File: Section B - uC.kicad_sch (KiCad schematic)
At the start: 9 parts, among them J1 Conn_ARM_SWD_TagConnect_TC203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, U1 ATtiny204-SS

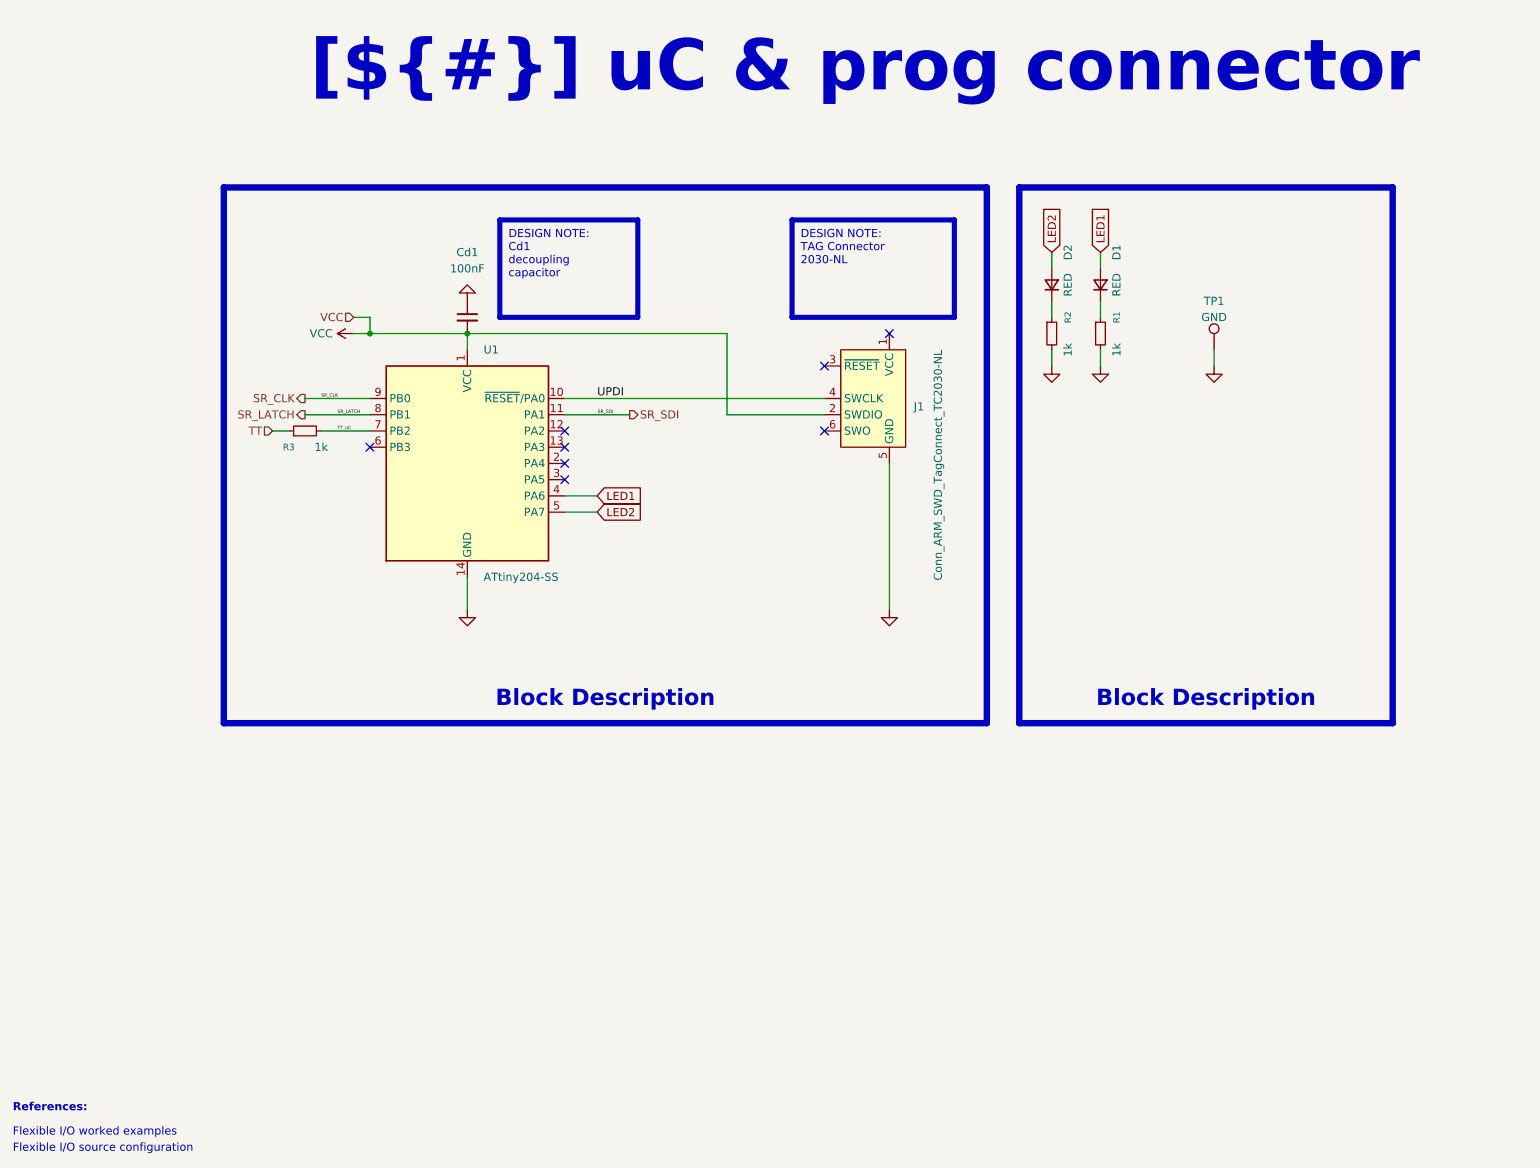
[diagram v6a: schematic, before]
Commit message: documentation update / block diagram
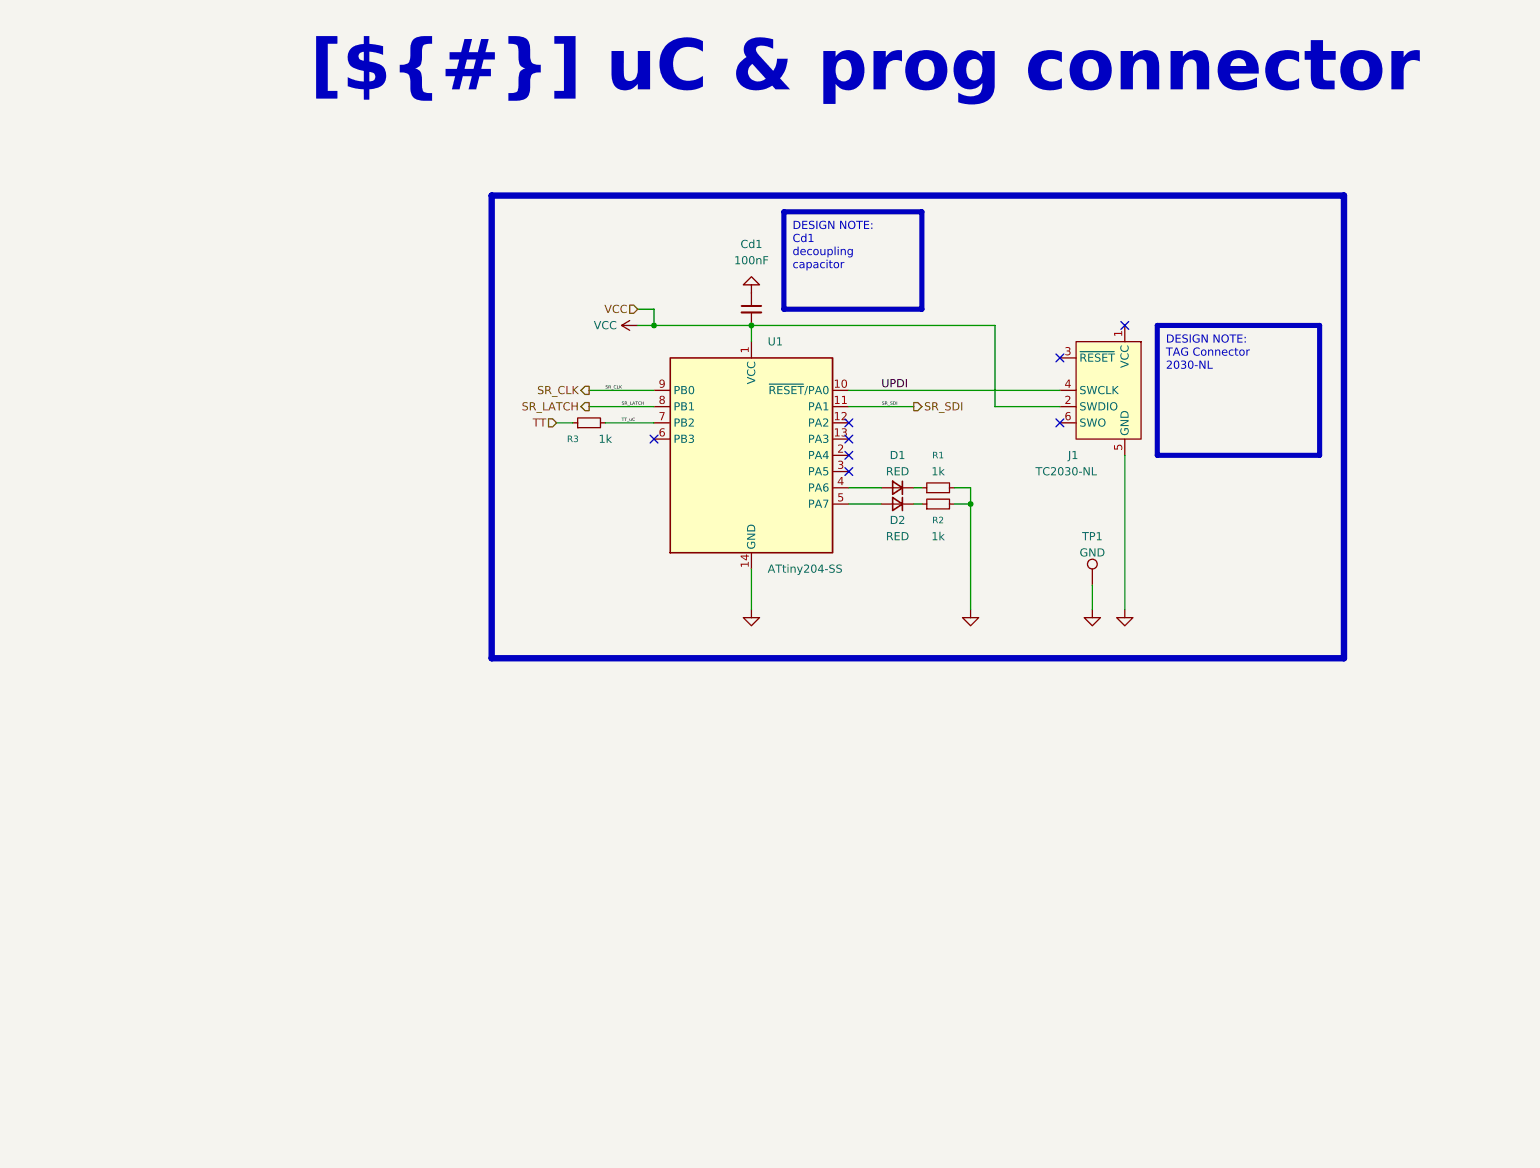
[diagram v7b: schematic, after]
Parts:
- J1: value Conn_ARM_SWD_TagConnect_TC2030-NL -> TC2030-NL
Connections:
- net LED1: no longer names the net of D1.2 (A), U1.4 (PA6)
- net LED2: no longer names the net of D2.2 (A), U1.5 (PA7)
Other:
- note removed: "Flexible I/O source configuration"
- note removed: "Flexible I/O worked examples"
- note removed: "References:"
- moved on the sheet: Cd1, D1, D2, J1, R1, R2, R3, TP1, U1
